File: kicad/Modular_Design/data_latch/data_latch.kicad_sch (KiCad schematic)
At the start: 4 parts

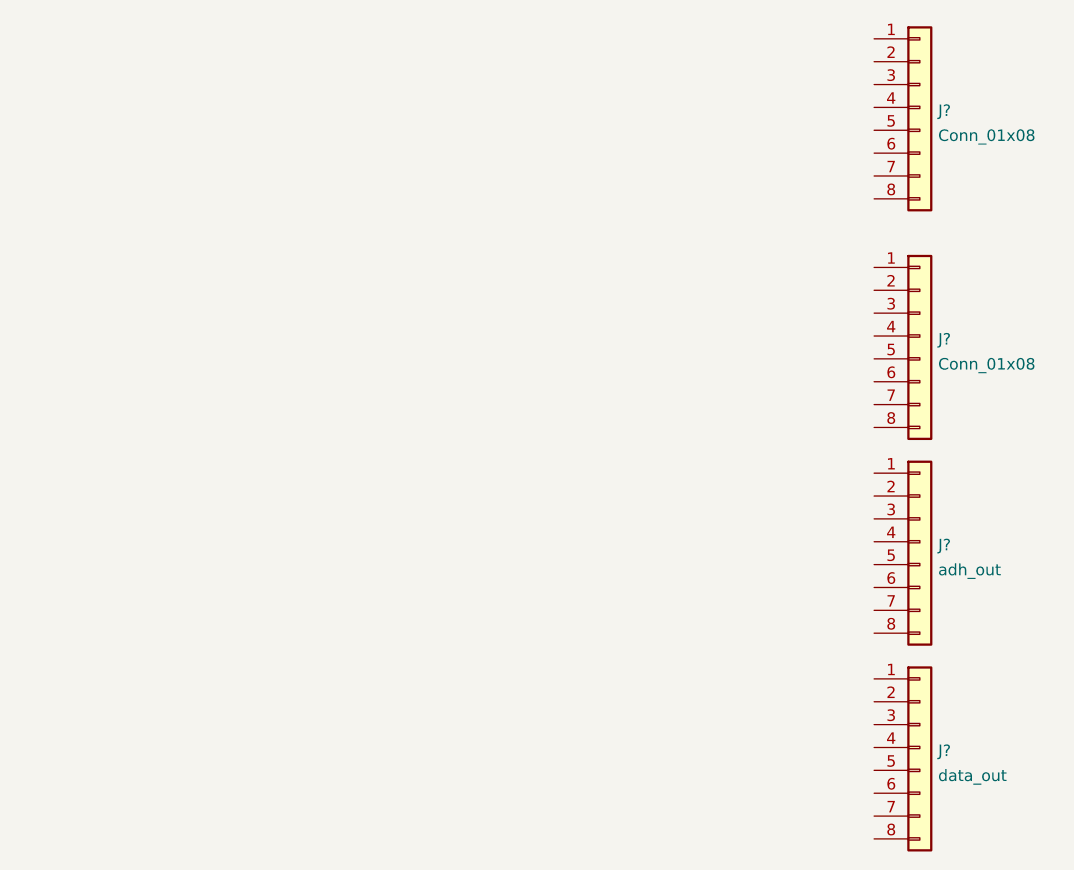
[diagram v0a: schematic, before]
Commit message: changes data_latch
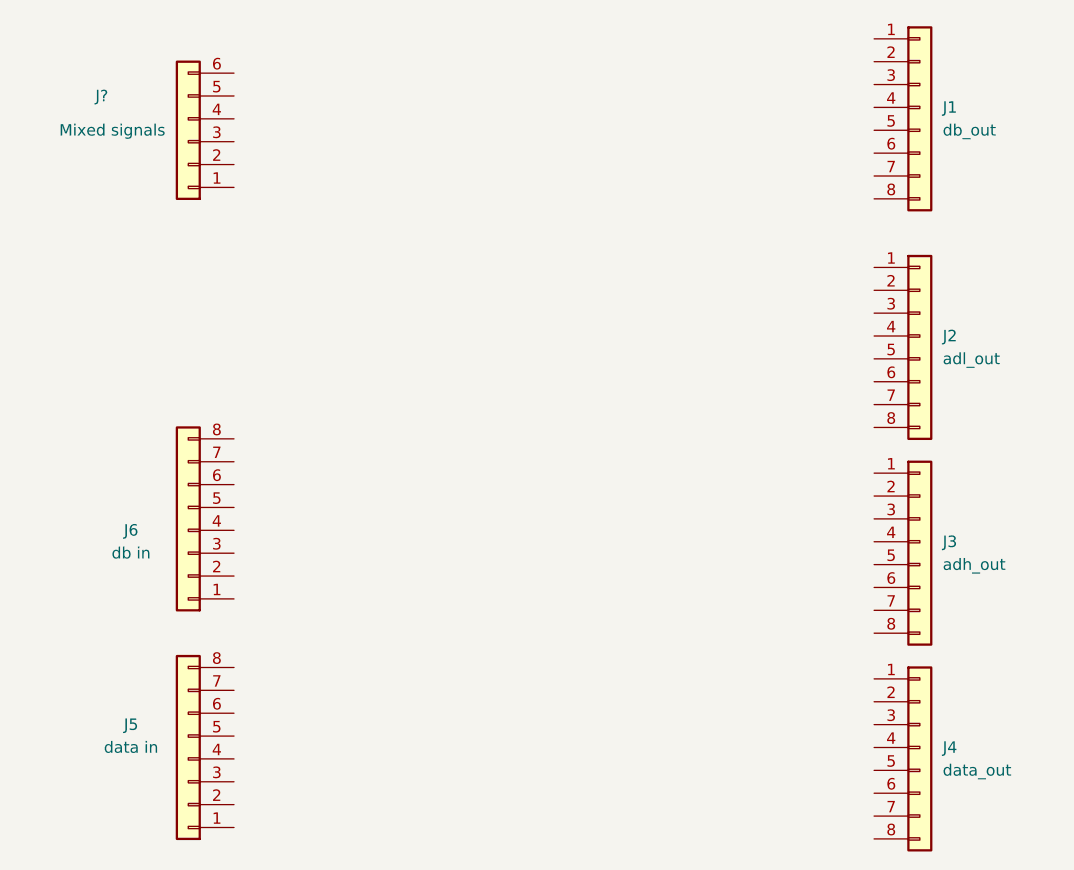
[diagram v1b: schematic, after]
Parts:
- added J5: data in, symbol Connector_Generic:Conn_01x08
- added J6: db in, symbol Connector_Generic:Conn_01x08
- added J?: Mixed signals, symbol Connector_Generic:Conn_01x06
- J1: renamed from J?; value Conn_01x08 -> db_out
- J2: renamed from J?; value Conn_01x08 -> adl_out
- gave numbers to parts that had none: 2
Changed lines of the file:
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@@
   (symbol (lib_id "Connector_Generic:Conn_01x08") (at 198.12 88.9 0) (unit 1)
     (in_bom yes) (on_board yes) (fields_autoplaced)
-    (property "Reference" "J?" (id 0) (at 200.152 89.2615 0)
+    (property "Reference" "J3" (id 0) (at 200.66 88.8999 0)
       (effects (font (size 1.27 1.27)) (justify left))
     )
-    (property "Value" "adh_out" (id 1) (at 200.152 92.0366 0)
+    (property "Value" "adh_out" (id 1) (at 200.66 91.4399 0)
       (effects (font (size 1.27 1.27)) (justify left))
     )
@@
   (symbol (lib_id "Connector_Generic:Conn_01x08") (at 198.12 111.76 0) (unit 1)
     (in_bom yes) (on_board yes) (fields_autoplaced)
-    (property "Reference" "J?" (id 0) (at 200.152 112.1215 0)
+    (property "Reference" "J4" (id 0) (at 200.66 111.7599 0)
       (effects (font (size 1.27 1.27)) (justify left))
     )
-    (property "Value" "data_out" (id 1) (at 200.152 114.8966 0)
+    (property "Value" "data_out" (id 1) (at 200.66 114.2999 0)
       (effects (font (size 1.27 1.27)) (justify left))
     )
@@
     (pin "8")
   )
+  (symbol (lib_id "Connector_Generic:Conn_01x06") (at 116.84 44.45 180) (unit 1)
+    (in_bom yes) (on_board yes)
+    (property "Reference" "J?" (id 0) (at 107.95 39.37 0)
+      (effects (font (size 1.27 1.27)) (justify left))
+    )
+    (property "Value" "Mixed signals" (id 1) (at 114.3 43.18 0)
+      (effects (font (size 1.27 1.27)) (justify left))
+    )
+    (property "Footprint" "" (id 2) (at 116.84 44.45 0)
+      (effects (font (size 1.27 1.27)) hide)
+    )
+    (property "Datasheet" "~" (id 3) (at 116.84 44.45 0)
+      (effects (font (size 1.27 1.27)) hide)
+    )
+    (pin "1")
+    (pin "2")
+    (pin "3")
+    (pin "4")
+    (pin "5")
+    (pin "6")
+  )
+  (symbol (lib_id "Connector_Generic:Conn_01x08") (at 116.84 87.63 180) (unit 1)
+    (in_bom yes) (on_board yes)
+    (property "Reference" "J6" (id 0) (at 110.49 87.63 0))
+    (property "Value" "db in" (id 1) (at 110.49 90.17 0))
+    (property "Footprint" "" (id 2) (at 116.84 87.63 0)
+      (effects (font (size 1.27 1.27)) hide)
+    )
+    (property "Datasheet" "~" (id 3) (at 116.84 87.63 0)
+      (effects (font (size 1.27 1.27)) hide)
+    )
+    (pin "1")
+    (pin "2")
+    (pin "3")
+    (pin "4")
+    (pin "5")
+    (pin "6")
+    (pin "7")
+    (pin "8")
+  )
   (symbol (lib_id "Connector_Generic:Conn_01x08") (at 198.12 66.04 0) (unit 1)
     (in_bom yes) (on_board yes) (fields_autoplaced)
-    (property "Reference" "J?" (id 0) (at 200.152 66.4015 0)
+    (property "Reference" "J2" (id 0) (at 200.66 66.0399 0)
       (effects (font (size 1.27 1.27)) (justify left))
     )
-    (property "Value" "Conn_01x08" (id 1) (at 200.152 69.1766 0)
+    (property "Value" "adl_out" (id 1) (at 200.66 68.5799 0)
       (effects (font (size 1.27 1.27)) (justify left))
     )
@@
   (symbol (lib_id "Connector_Generic:Conn_01x08") (at 198.12 40.64 0) (unit 1)
     (in_bom yes) (on_board yes) (fields_autoplaced)
-    (property "Reference" "J?" (id 0) (at 200.152 41.0015 0)
+    (property "Reference" "J1" (id 0) (at 200.66 40.6399 0)
       (effects (font (size 1.27 1.27)) (justify left))
     )
-    (property "Value" "Conn_01x08" (id 1) (at 200.152 43.7766 0)
+    (property "Value" "db_out" (id 1) (at 200.66 43.1799 0)
       (effects (font (size 1.27 1.27)) (justify left))
     )
@@
     (pin "8")
   )
+  (symbol (lib_id "Connector_Generic:Conn_01x08") (at 116.84 113.03 180) (unit 1)
+    (in_bom yes) (on_board yes)
+    (property "Reference" "J5" (id 0) (at 110.49 109.22 0))
+    (property "Value" "data in" (id 1) (at 110.49 111.76 0))
+    (property "Footprint" "" (id 2) (at 116.84 113.03 0)
+      (effects (font (size 1.27 1.27)) hide)
+    )
+    (property "Datasheet" "~" (id 3) (at 116.84 113.03 0)
+      (effects (font (size 1.27 1.27)) hide)
+    )
+    (pin "1")
+    (pin "2")
+    (pin "3")
+    (pin "4")
+    (pin "5")
+    (pin "6")
+    (pin "7")
+    (pin "8")
+  )
   (sheet_instances
     (path "/" (page "1"))
   )
   (symbol_instances
+    (path "/bbb99edd-f016-43ea-b1c7-0bcdd1915ee8"
+      (reference "J1") (unit 1) (value "db_out") (footprint "")
+    )
+    (path "/87d12864-a0e8-4310-9a66-a8b9c6099da4"
+      (reference "J2") (unit 1) (value "adl_out") (footprint "")
+    )
     (path "/0177b717-8f7d-4b62-97bb-d5eac4a4019b"
-      (reference "J?") (unit 1) (value "adh_out") (footprint "")
+      (reference "J3") (unit 1) (value "adh_out") (footprint "")
     )
     (path "/0853099b-f4f4-4426-be1e-a87c35a3a3de"
-      (reference "J?") (unit 1) (value "data_out") (footprint "")
+      (reference "J4") (unit 1) (value "data_out") (footprint "")
     )
-    (path "/87d12864-a0e8-4310-9a66-a8b9c6099da4"
-      (reference "J?") (unit 1) (value "Conn_01x08") (footprint "")
+    (path "/dfd6675d-4c2b-44c2-b161-80303193ec6b"
+      (reference "J5") (unit 1) (value "data in") (footprint "")
     )
-    (path "/bbb99edd-f016-43ea-b1c7-0bcdd1915ee8"
-      (reference "J?") (unit 1) (value "Conn_01x08") (footprint "")
+    (path "/55db04cb-8f36-4940-9aa1-d84d545e7264"
+      (reference "J6") (unit 1) (value "db in") (footprint "")
+    )
+    (path "/43a5bd49-9da0-4dc6-8831-c4b31f45dae9"
+      (reference "J?") (unit 1) (value "Mixed signals") (footprint "")
     )
   )
